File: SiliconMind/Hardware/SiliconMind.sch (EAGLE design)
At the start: 38 parts, among them IC1 LM358, Q1 20MHz, U1 328P, U2 MCP4921PDIP, U3 7805, U4 QUAD_OPAMP

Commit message: added micro match connector
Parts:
- added X1: MICROMATCH-20, con-amp-micromatch:MICROMATCH-20
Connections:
- net TRIG renamed N$17
- removed net B_TRIG: U1.PD3(INT1)
- removed net SCL: U1.PC5(ADC5/SCL)
- removed net SDA: U1.PC4(ADC4/SDA)
- removed net T8: U1.PD7(AIN1)
- new net T0: U1.PC0(ADC0)
- net T1: now also U1.PC1(ADC1); no longer U1.PD5(T1)
- net T2: now also U1.PC2(ADC2); no longer U1.PD4(XCK/T0)
- net T3: now also U1.PC3(ADC3); no longer U1.PC2(ADC2)
- net T4: now also U1.PC4(ADC4/SDA); no longer U1.PC3(ADC3)
- net T5: now also U1.PC5(ADC5/SCL); no longer U1.PC0(ADC0)
- net T6: now also U1.PD0(RXD); no longer U1.PC1(ADC1)
- net T7: now also U1.PD1(TXD); no longer U1.PD6(AIN0)
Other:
- note added: "Silocon Mind from the Workshop of Telescopes Prototype keyboard connector"
- note removed: "Silocon Mind from the Workshop of Telescopes"

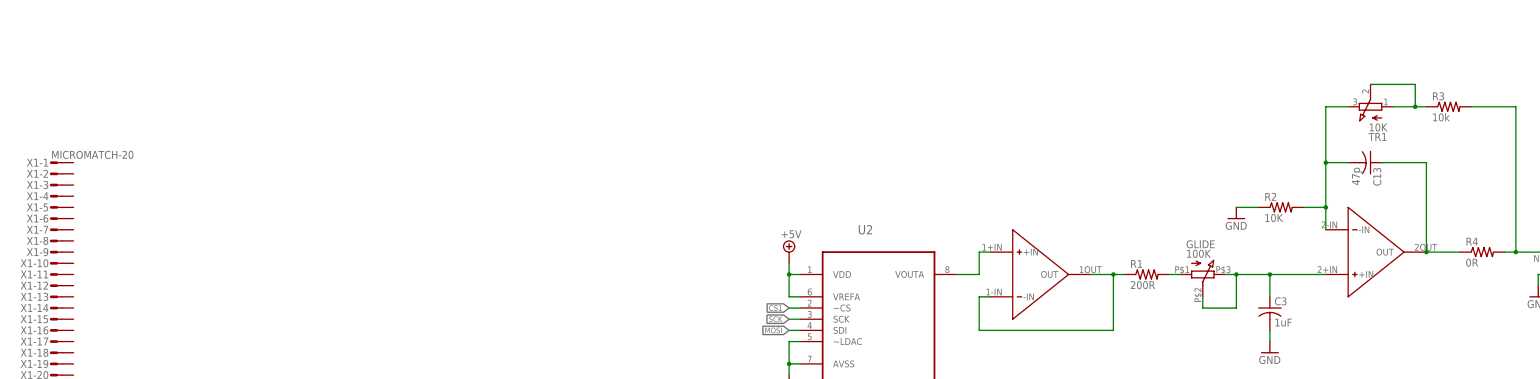
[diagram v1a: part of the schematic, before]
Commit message: Changed TL074 to TTL
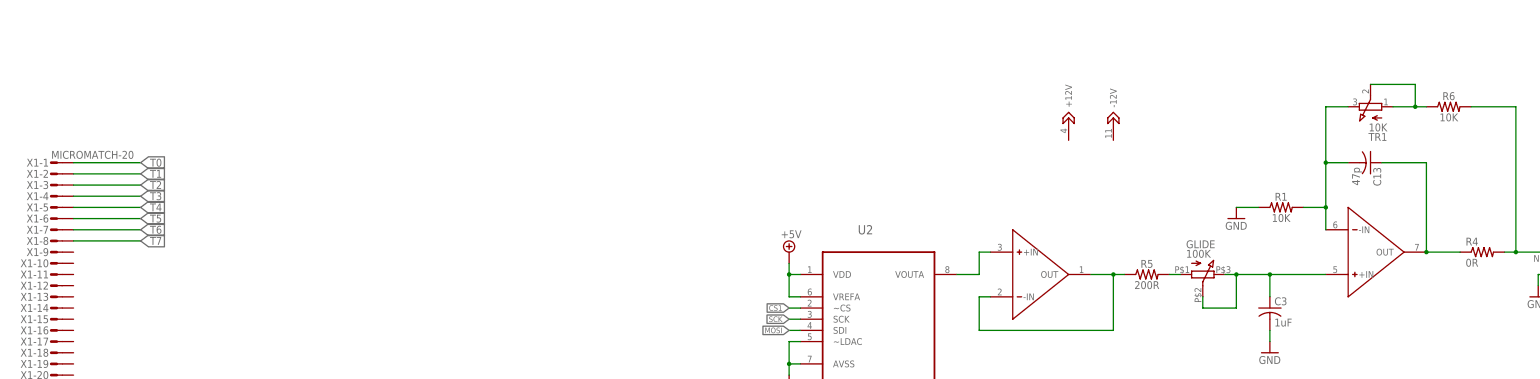
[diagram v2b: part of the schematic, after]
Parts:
- removed R2: 10K, rcl:R-US_R0805
- removed R3: 10k, rcl:R-US_R0805
- added R5: 200R, SparkFun-Resistors:RESISTORAXIAL-0.3
- added R6: 10K, SparkFun-Resistors:RESISTORAXIAL-0.3
- R1: value 200R -> 10K; device rcl:R-US_R0805 -> SparkFun-Resistors:RESISTORAXIAL-0.3
- U4: value QUAD_OPAMP -> (none); device INSTRUO:QUAD_OPAMP -> INSTRUO:QUAD_OPAMPDIP14
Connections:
- net GND: now also R1.1; no longer R2.1
- net N$12: now also R1.2; no longer R2.2
- net N$4: now also R5.1; no longer R1.1
- net N$5: now also R5.2; no longer R1.2
- net N$7: now also R6.1; no longer R3.1
- net N$8: now also R6.2; no longer R3.2
- net T0: now also X1-1.S
- net T1: now also X1-2.S
- net T2: now also X1-3.S
- net T3: now also X1-4.S
- net T4: now also X1-5.S
- net T5: now also X1-6.S
- net T6: now also X1-7.S
- net T7: now also X1-8.S
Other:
- moved on the sheet: R1

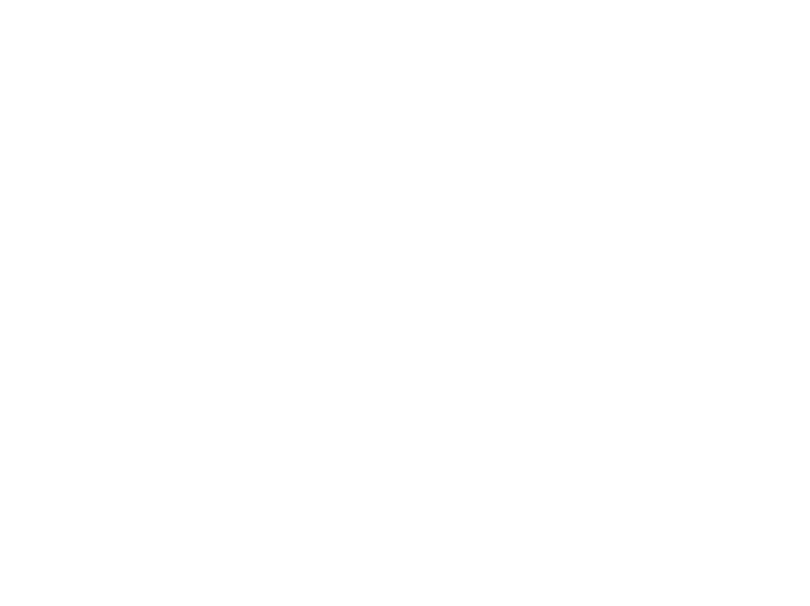
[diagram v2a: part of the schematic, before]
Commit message: added IDC connector
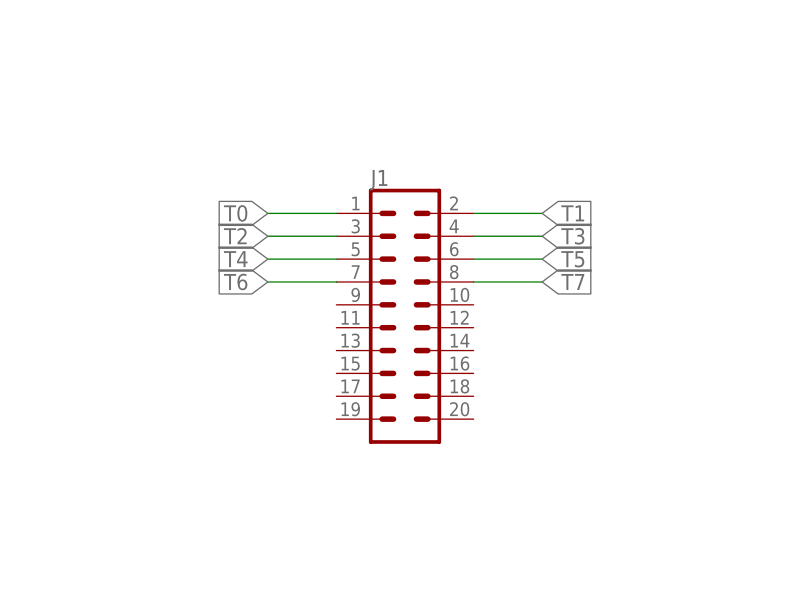
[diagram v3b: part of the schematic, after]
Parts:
- added J1: (no value), SparkFun-Connectors:CONN_10X2
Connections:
- net T0: now also J1.1
- net T1: now also J1.2
- net T2: now also J1.3
- net T3: now also J1.4
- net T4: now also J1.5
- net T5: now also J1.6
- net T6: now also J1.7
- net T7: now also J1.8
